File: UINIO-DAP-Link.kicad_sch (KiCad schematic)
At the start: 0 parts

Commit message: Start schematic drawing work.
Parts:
- added C1: 10nF, Capacitor_SMD:C_0402_1005Metric, symbol Uinio:CAP_0402
- added C2: 10uF, Capacitor_SMD:C_0402_1005Metric, symbol Uinio:CAP_0402
- added C3, C4: 20pF, symbol Device:C
- added J1: Conn_01x04_Male, symbol Connector:Conn_01x04_Male
- added J2, J?: Conn_02x05_Top_Bottom, symbol Connector_Generic:Conn_02x05_Top_Bottom
- added J?: Conn_02x10_Top_Bottom, symbol Connector_Generic:Conn_02x10_Top_Bottom
- added R1, R2, R3, R5: 10K, symbol Device:R
- added R4: 100R, symbol Device:R
- added U1: ME6211, Uinio:SOT-23-5_L3.0-W1.7-P0.95-LS2.8-BR, symbol Uinio:ME6211
- added U2: STM32F103C8T6, kicad_lceda:LQFP-48_L7.0-W7.0-P0.50-LS9.0-BL, symbol Uinio:STM32F103C8T6
- added USB1: USB_Type_C_16Pin, Uinio:USB-C-SMD_TYPEC-304J-BCP16, symbol Uinio:USB_Type_C_16Pin
- added Y1: Crystal_GND24, symbol Device:Crystal_GND24
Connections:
- new net: C1.2, U1.4 (NC)
- new net: U2.6 (PD1-OSC_OUT), Y1.1
- new net: C3.2, Y1.2
- new net: U2.5 (PD0-OSC_IN), Y1.3
- new net: C4.2, Y1.4
- new net: R3.1, U2.7 (NRST)
- new net: R4.2, U2.25 (PB12)
- new net: R5.1, U2.44 (BOOT0)
- new net BOOT1: R2.1, U2.20 (PB2)
- new net Download_SWCLK: J1.2 (Pin_2), U2.37 (PA14)
- new net Download_SWDIO: J1.3 (Pin_3), U2.34 (PA13)
- new net GND: C1.1, C2.1, C3.1, C4.1, J1.1 (Pin_1), J2.7 (Pin_7), J?.12 (Pin_12), J?.13 (Pin_13), J?.14 (Pin_14), J?.15 (Pin_15), J?.16 (Pin_16), J?.17 (Pin_17), J?.18 (Pin_18), J?.19 (Pin_19), J?.20 (Pin_20), J?.7 (Pin_7), R2.2, R5.2, U1.2 (Vss), U2.23 (VSS_1), U2.35 (VSS_2), U2.47 (VSS_3), U2.8 (VSSA), USB1.13 (GND), USB1.14 (GND), USB1.15 (GND), USB1.16 (GND), USB1.A1B12 (GND), USB1.B1A12 (GND)
- new net JTAG_TCK/SWCLK: J2.6 (Pin_6), U2.26 (PB13)
- new net JTAG_TDI: J2.5 (Pin_5), U2.17 (PA7)
- new net JTAG_TDO: J2.4 (Pin_4), U2.15 (PA5)
- new net JTAG_TMS/SWDIO: J2.8 (Pin_8), R4.1, U2.27 (PB14)
- new net JTAG_nTRST: J2.3 (Pin_3), R1.1, U2.18 (PB0)
- new net LED_BLUE: U2.42 (PB6)
- new net LED_RED: U2.30 (PA9)
- new net RESET: J?.8 (Pin_8)
- new net RTCK: J?.6 (Pin_6)
- new net TCK: J?.5 (Pin_5)
- new net TDI: J?.3 (Pin_3)
- new net TDO: J?.7 (Pin_7)
- new net TMS: J?.4 (Pin_4)
- new net USART2_RX: J2.2 (Pin_2), U2.13 (PA3)
- new net USART2_TX: J2.1 (Pin_1), U2.12 (PA2)
- new net USB_Data_N: U2.32 (PA11), USB1.A7 (DN1), USB1.B7 (DN2)
- new net USB_Data_P: U2.33 (PA12), USB1.A6 (DP1), USB1.B6 (DP2)
- new net USB_ENUM: U2.28 (PB15)
- new net VDD_3.3V: C2.2, J1.4 (Pin_4), J2.9 (Pin_9), R1.2, R3.2, U1.5 (Vout), U2.1 (VBAT), U2.24 (VDD_1), U2.36 (VDD_2), U2.48 (VDD_3), U2.9 (VDDA)
- new net VDD_5V: J2.10 (Pin_10), U1.1 (Vin), U1.3 (CE), USB1.A4B9 (VBUS), USB1.B4A9 (VBUS)
- new net VTref: J?.1 (Pin_1)
- new net _JTAG_TCK/SWCLK: J?.6 (Pin_6)
- new net _JTAG_TDI: J?.5 (Pin_5)
- new net _JTAG_TDO: J?.4 (Pin_4)
- new net _JTAG_TMS/SWDIO: J?.8 (Pin_8)
- new net _JTAG_nTRST: J?.3 (Pin_3)
- new net _USART2_RX: J?.2 (Pin_2)
- new net _USART2_TX: J?.1 (Pin_1)
- new net _VDD_3.3V: J?.9 (Pin_9)
- new net _VDD_5V: J?.10 (Pin_10)
- new net nTRST: J?.2 (Pin_2)
- no-connect marks 0 -> 25
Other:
- note added: "DAPLink 固件下载接口"
- note added: "JTAG/SWD 下载接口"
- note added: "ME6211 线性稳压器"
- note added: "STM32F103C8T6 最小系统"
- note added: "USB Type-C 接口"

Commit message: Update extends board design.
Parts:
- added D?: BLUE LED, symbol Device:LED
- added D? (x2): Blue LED, symbol Device:LED
- added J?: Conn_01x05_Male, symbol Connector:Conn_01x05_Male
- added J? (x2): Conn_01x02_Male, symbol Connector:Conn_01x02_Male
- added R? (x3): 1.5K, symbol Device:R
- added R? (x2): 22R, symbol Device:R
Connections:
- net GND: now also J?.9 (Pin_9), J?.1 (Pin_1), R?.1; no longer J?.7 (Pin_7)
- net _JTAG_TCK/SWCLK: now also J?.10 (Pin_10); no longer J?.6 (Pin_6)
- net _JTAG_TDI: now also R?.1; no longer J?.5 (Pin_5)
- net _JTAG_TDO: now also R?.1; no longer J?.4 (Pin_4)
- net _USART2_RX: now also J?.4 (Pin_4), J?.2 (Pin_2), R?.2; no longer J?.2 (Pin_2)
- net _USART2_TX: now also J?.5 (Pin_5), J?.3 (Pin_3), R?.2; no longer J?.1 (Pin_1)
- net _VDD_3.3V: now also J?.7 (Pin_7); no longer J?.9 (Pin_9)
- net _VDD_5V: now also J?.6 (Pin_6); no longer J?.10 (Pin_10)
- net _JTAG_nTRST renamed _JTAG_nTRST_Output
- new net: D?.1 (K), R?.2
- new net: J?.1 (Pin_1), R?.2
- new net: J?.2 (Pin_2), R?.2
- new net: D?.1 (K), R?.1 (x2)
- new net 3.3V_Input: D?.2 (A), D?.2 (A), D?.2 (A), J?.4 (Pin_4)
- new net 5V: J?.5 (Pin_5)
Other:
- note added: "3.3V_Input"
- note added: "3.3V_Output"
- moved on the sheet: C1, C2, C3, C4, J1, J2, J?, R1, R2, R3, R4, R5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

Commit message: Update PCB.
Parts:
- removed C1: 10nF, Capacitor_SMD:C_0402_1005Metric, symbol Uinio:CAP_0402
- removed C2: 10uF, Capacitor_SMD:C_0402_1005Metric, symbol Uinio:CAP_0402
- added C1: 10nF, Capacitor_SMD:C_0603_1608Metric, symbol Device:C
- added C2: 10uF, Capacitor_SMD:C_0603_1608Metric, symbol Device:C
- added C?: 0.1uF, Capacitor_SMD:C_0603_1608Metric, symbol Device:C
- C3, C4: footprint (none) -> Capacitor_SMD:C_0603_1608Metric
- D1: renamed from D?; value Blue LED -> LED Red; footprint (none) -> Capacitor_SMD:C_0603_1608Metric
- D2: renamed from D?; value Blue LED -> LED Blue; footprint (none) -> Capacitor_SMD:C_0603_1608Metric
- D3: renamed from D?; value BLUE LED -> LED Blue; footprint (none) -> Capacitor_SMD:C_0603_1608Metric
- J1: renamed from J?; footprint (none) -> Connector_PinHeader_2.54mm:PinHeader_1x05_P2.54mm_Vertical
- J2: renamed from J?; value Conn_02x10_Top_Bottom -> JTAG 输出; footprint (none) -> Connector_PinHeader_2.54mm:PinHeader_2x10_P2.54mm_Vertical
- J3: renamed from J?; value Conn_01x02_Male -> JTAG_nTRST 跳线选择; footprint (none) -> Connector_PinHeader_2.54mm:PinHeader_1x02_P2.54mm_Vertical
- J4: renamed from J?; value Conn_01x02_Male -> 3.3V 跳线选择; footprint (none) -> Connector_PinHeader_2.54mm:PinHeader_1x02_P2.54mm_Vertical
- J5: renamed from J?; value Conn_02x05_Top_Bottom -> SWD 输入; footprint (none) -> Connector_PinHeader_2.54mm:PinHeader_2x05_P2.54mm_Vertical
- J6: renamed from J1; value Conn_01x04_Male -> DAPLink 固件下载接口; footprint (none) -> Connector:FanPinHeader_1x04_P2.54mm_Vertical
- J7: renamed from J2; value Conn_02x05_Top_Bottom -> JTAG/SWD 下载接口; footprint (none) -> Connector_PinHeader_2.54mm:PinHeader_2x05_P2.54mm_Vertical
- R1, R2, R3, R4, R5: renamed from R?; footprint (none) -> Resistor_SMD:R_0603_1608Metric
- R10: renamed from R5; footprint (none) -> Resistor_SMD:R_0603_1608Metric
- R6: renamed from R1; footprint (none) -> Resistor_SMD:R_0603_1608Metric
- R7: renamed from R2; footprint (none) -> Resistor_SMD:R_0603_1608Metric
- R8: renamed from R3; footprint (none) -> Resistor_SMD:R_0603_1608Metric
- R9: renamed from R4; footprint (none) -> Resistor_SMD:R_0603_1608Metric
- U1: renamed from U2; footprint kicad_lceda:LQFP-48_L7.0-W7.0-P0.50-LS9.0-BL -> Uinio:LQFP-48_L7.0-W7.0-P0.50-LS9.0
- Y1: footprint (none) -> Crystal:Crystal_SMD_0603-4Pin_6.0x3.5mm
- renumbered U1 to V1
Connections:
- net 3.3V_Input: now also J4.1 (Pin_1)
- net GND: now also C1.1, C2.2, C?.2
- net VDD_3.3V: now also C2.1
- net _JTAG_nTRST_Output: now also J3.2 (Pin_2)
- net at V1.4 (NC): now also C1.2
- net at R8.1, U1.7 (NRST): now also C?.1
- net _JTAG_nTRST_Input: now reaches J3.1 (Pin_1)
- net 3.3V_Output: now reaches J2.11 (Pin_11)
- net 3.3V_Output: now also J4.2 (Pin_2)
- net LED_BLUE renamed LED Red
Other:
- note added: "JTAG 扩展板"
- note removed: "3.3V_Input"
- note removed: "3.3V_Output"
- moved on the sheet: D1, D2, D3, J3, J4, J5, J6, J7, R1, R2, R3, R4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

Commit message: Update PCB layout.
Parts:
- added D4: LED_Blue, LED_SMD:LED_0603_1608Metric, symbol Device:LED
- added D5: LED_Red, LED_SMD:LED_0603_1608Metric, symbol Device:LED
- added R11, R12: 10K, Resistor_SMD:R_0603_1608Metric, symbol Device:R
- D1: value LED Red -> LED_Red; footprint Capacitor_SMD:C_0603_1608Metric -> LED_SMD:LED_0603_1608Metric
- D2, D3: value LED Blue -> LED_Blue; footprint Capacitor_SMD:C_0603_1608Metric -> LED_SMD:LED_0603_1608Metric
- J1: value Conn_01x05_Male -> 扩展板串口 & 电源输出
- J2: value JTAG 输出 -> 扩展板 JTAG 输出; footprint Connector_PinHeader_2.54mm:PinHeader_2x10_P2.54mm_Vertical -> Connector_IDC:IDC-Header_2x10_P2.54mm_Horizontal
- J5: value SWD 输入 -> 扩展板 SWD 输入; footprint Connector_PinHeader_2.54mm:PinHeader_2x05_P2.54mm_Vertical -> Connector_IDC:IDC-Header_2x05_P2.54mm_Horizontal
- J6: footprint Connector:FanPinHeader_1x04_P2.54mm_Vertical -> Connector_PinHeader_2.54mm:PinHeader_1x04_P2.54mm_Vertical
- J7: footprint Connector_PinHeader_2.54mm:PinHeader_2x05_P2.54mm_Vertical -> Connector_IDC:IDC-Header_2x05_P2.54mm_Horizontal
- gave numbers to parts that had none: 1
- renumbered R8 to R6, R6 to R7, R7 to R8, V1 to U1, U1 to U2
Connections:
- net GND: now also R11.2, R12.2
- net LED Red: no longer names the net of U2.42 (PB6)
- net LED Red: now also D4.2 (A)
- net LED_RED: no longer names the net of U2.30 (PA9)
- net LED_RED: now also D5.2 (A)
- new net: D4.1 (K), R11.1
- new net: D5.1 (K), R12.1
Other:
- note added: "DAPLink 固件下载"
- note added: "SWD/JTAG 输出"
- note removed: "DAPLink 固件下载接口"
- note removed: "JTAG/SWD 下载接口"

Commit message: Update PCB layout.
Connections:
- net RESET is gone; now on net _JTAG_nTRST_Output: J2.8 (Pin_8)
- net TCK is gone; now on net _JTAG_TCK/SWCLK: J2.5 (Pin_5)
- net TDI is gone; now on net _JTAG_TDI: J2.3 (Pin_3)
- net TDO is gone; now on net _JTAG_TDO: J2.7 (Pin_7)
- net TMS is gone; now on net _JTAG_TMS/SWDIO: J2.4 (Pin_4)
- net VTref is gone; now on net 3.3V_Output: J2.1 (Pin_1)
- no-connect marks 25 -> 27
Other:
- moved on the sheet: J2, J3, J4, R4, R5

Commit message: Update PCB layout.
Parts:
- removed J5: 扩展板 SWD 输入, Connector_IDC:IDC-Header_2x05_P2.54mm_Horizontal, symbol Connector_Generic:Conn_02x05_Top_Bottom
- removed J7: JTAG/SWD 下载接口, Connector_IDC:IDC-Header_2x05_P2.54mm_Horizontal, symbol Connector_Generic:Conn_02x05_Top_Bottom
- added J5: 扩展板 SWD 输入, Connector_IDC:IDC-Header_2x05_P2.54mm_Horizontal, symbol Connector_Generic:Conn_02x05_Odd_Even
- added J7: JTAG/SWD 下载接口, Connector_IDC:IDC-Header_2x05_P2.54mm_Horizontal, symbol Connector_Generic:Conn_02x05_Odd_Even
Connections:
- net GND: now also J5.4 (Pin_4), J7.8 (Pin_8)
- net JTAG_TCK/SWCLK: now also J7.10 (Pin_10)
- net JTAG_TDI: now also J7.1 (Pin_1)
- net JTAG_TDO: now also J7.3 (Pin_3)
- net JTAG_TMS/SWDIO: now also J7.6 (Pin_6)
- net JTAG_nTRST: now also J7.5 (Pin_5)
- net USART2_RX: now also J7.7 (Pin_7)
- net USART2_TX: now also J7.9 (Pin_9)
- net VDD_3.3V: now also J7.4 (Pin_4)
- net VDD_5V: now also J7.2 (Pin_2)
- net _JTAG_TCK/SWCLK: now also J5.2 (Pin_2)
- net _JTAG_TMS/SWDIO: now also J5.6 (Pin_6)
- net _JTAG_nTRST_Output: now also J5.5 (Pin_5)
- net _USART2_RX: now also J5.3 (Pin_3)
- net _USART2_TX: now also J5.1 (Pin_1)
- net _VDD_3.3V: now also J5.8 (Pin_8)
- net _VDD_5V: now also J5.10 (Pin_10)
- net at R5.2: now also J5.9 (Pin_9)
- net at R4.2: now also J5.7 (Pin_7)
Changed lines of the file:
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@@
-    (stroke (width 0) (type default) (color 0 0 0 0))
-  )
-  (wire (pts (xy 128.27 175.26) (xy 121.92 175.26))
     (stroke (width 0) (type default) (color 0 0 0 0))
   )
@@
   )
   (wire (pts (xy 53.975 143.51) (xy 56.515 143.51))
+    (stroke (width 0) (type default) (color 0 0 0 0))
+  )
+  (wire (pts (xy 109.22 167.64) (xy 128.27 167.64))
     (stroke (width 0) (type default) (color 0 0 0 0))
   )
@@
     (stroke (width 0) (type default) (color 0 0 0 0))
   )
-  (wire (pts (xy 109.22 170.18) (xy 128.27 170.18))
-    (stroke (width 0) (type default) (color 0 0 0 0))
-  )
   (polyline (pts (xy 17.78 130.81) (xy 114.3 130.81))
     (stroke (width 0) (type default) (color 0 0 0 0))
@@
     (stroke (width 0) (type default) (color 0 0 0 0))
   )
+  (wire (pts (xy 124.46 177.8) (xy 128.27 177.8))
+    (stroke (width 0) (type default) (color 0 0 0 0))
+  )
   (wire (pts (xy 236.22 104.14) (xy 243.84 104.14))
     (stroke (width 0) (type default) (color 0 0 0 0))
@@
     (stroke (width 0) (type default) (color 0 0 0 0))
   )
-  (wire (pts (xy 124.46 177.8) (xy 128.27 177.8))
-    (stroke (width 0) (type default) (color 0 0 0 0))
-  )
   (polyline (pts (xy 114.3 16.51) (xy 114.3 57.15))
     (stroke (width 0) (type default) (color 0 0 0 0))
@@
   )
   (wire (pts (xy 93.98 185.42) (xy 90.17 185.42))
+    (stroke (width 0) (type default) (color 0 0 0 0))
+  )
+  (wire (pts (xy 121.92 175.26) (xy 128.27 175.26))
     (stroke (width 0) (type default) (color 0 0 0 0))
   )
@@
     (stroke (width 0) (type default) (color 0 0 0 0))
   )
+  (wire (pts (xy 109.22 170.18) (xy 128.27 170.18))
+    (stroke (width 0) (type default) (color 0 0 0 0))
+  )
   (wire (pts (xy 236.22 109.22) (xy 243.84 109.22))
     (stroke (width 0) (type default) (color 0 0 0 0))
   )
   (wire (pts (xy 93.98 172.72) (xy 93.98 185.42))
-    (stroke (width 0) (type default) (color 0 0 0 0))
-  )
-  (wire (pts (xy 109.22 167.64) (xy 128.27 167.64))
     (stroke (width 0) (type default) (color 0 0 0 0))
   )
@@
     (pin "4")
   )
-  (symbol (lib_id "power:GND") (at 242.57 76.2 90) (unit 1)
-    (in_bom yes) (on_board yes)
-    (property "Reference" "#PWR019" (id 0) (at 248.92 76.2 0)
-      (effects (font (size 1.27 1.27)) hide)
-    )
-    (property "Value" "GND" (id 1) (at 245.872 76.2 90)
-      (effects (font (size 1.27 1.27)) (justify right))
-    )
-    (property "Footprint" "" (id 2) (at 242.57 76.2 0)
-      (effects (font (size 1.27 1.27)) hide)
-    )
-    (property "Datasheet" "" (id 3) (at 242.57 76.2 0)
-      (effects (font (size 1.27 1.27)) hide)
-    )
-    (pin "1")
-  )
-  (symbol (lib_id "power:GND") (at 191.77 129.54 270) (unit 1)
-    (in_bom yes) (on_board yes)
-    (property "Reference" "#PWR016" (id 0) (at 185.42 129.54 0)
-      (effects (font (size 1.27 1.27)) hide)
-    )
-    (property "Value" "GND" (id 1) (at 188.722 129.54 90)
-      (effects (font (size 1.27 1.27)) (justify right))
-    )
-    (property "Footprint" "" (id 2) (at 191.77 129.54 0)
-      (effects (font (size 1.27 1.27)) hide)
-    )
-    (property "Datasheet" "" (id 3) (at 191.77 129.54 0)
-      (effects (font (size 1.27 1.27)) hide)
-    )
-    (pin "1")
-  )
-  (symbol (lib_id "Connector_Generic:Conn_02x05_Top_Bottom") (at 133.35 172.72 0) (mirror x) (unit 1)
-    (in_bom yes) (on_board yes)
-    (property "Reference" "J5" (id 0) (at 134.62 180.34 0))
-    (property "Value" "扩展板 SWD 输入" (id 1) (at 134.62 162.56 0))
+  (symbol (lib_id "Connector_Generic:Conn_02x05_Odd_Even") (at 133.35 172.72 0) (unit 1)
+    (in_bom yes) (on_board yes)
+    (property "Reference" "J5" (id 0) (at 134.62 164.465 0))
+    (property "Value" "扩展板 SWD 输入" (id 1) (at 134.62 180.975 0))
     (property "Footprint" "Connector_IDC:IDC-Header_2x05_P2.54mm_Horizontal" (id 2) (at 133.35 172.72 0)
       (effects (font (size 1.27 1.27)) hide)
@@
     (pin "9")
   )
+  (symbol (lib_id "power:GND") (at 242.57 76.2 90) (unit 1)
+    (in_bom yes) (on_board yes)
+    (property "Reference" "#PWR019" (id 0) (at 248.92 76.2 0)
+      (effects (font (size 1.27 1.27)) hide)
+    )
+    (property "Value" "GND" (id 1) (at 245.872 76.2 90)
+      (effects (font (size 1.27 1.27)) (justify right))
+    )
+    (property "Footprint" "" (id 2) (at 242.57 76.2 0)
+      (effects (font (size 1.27 1.27)) hide)
+    )
+    (property "Datasheet" "" (id 3) (at 242.57 76.2 0)
+      (effects (font (size 1.27 1.27)) hide)
+    )
+    (pin "1")
+  )
+  (symbol (lib_id "power:GND") (at 191.77 129.54 270) (unit 1)
+    (in_bom yes) (on_board yes)
+    (property "Reference" "#PWR016" (id 0) (at 185.42 129.54 0)
+      (effects (font (size 1.27 1.27)) hide)
+    )
+    (property "Value" "GND" (id 1) (at 188.722 129.54 90)
+      (effects (font (size 1.27 1.27)) (justify right))
+    )
+    (property "Footprint" "" (id 2) (at 191.77 129.54 0)
+      (effects (font (size 1.27 1.27)) hide)
+    )
+    (property "Datasheet" "" (id 3) (at 191.77 129.54 0)
+      (effects (font (size 1.27 1.27)) hide)
+    )
+    (pin "1")
+  )
   (symbol (lib_id "power:GND") (at 88.9 95.25 90) (unit 1)
     (in_bom yes) (on_board yes)
@@
     (pin "1")
     (pin "2")
-  )
-  (symbol (lib_id "Connector_Generic:Conn_02x05_Top_Bottom") (at 231.14 34.29 0) (unit 1)
-    (in_bom yes) (on_board yes)
-    (property "Reference" "J7" (id 0) (at 232.41 25.4 0))
-    (property "Value" "JTAG/SWD 下载接口" (id 1) (at 232.41 43.18 0))
-    (property "Footprint" "Connector_IDC:IDC-Header_2x05_P2.54mm_Horizontal" (id 2) (at 231.14 34.29 0)
-      (effects (font (size 1.27 1.27)) hide)
-    )
-    (property "Datasheet" "~" (id 3) (at 231.14 34.29 0)
-      (effects (font (size 1.27 1.27)) hide)
-    )
-    (pin "1")
-    (pin "10")
-    (pin "2")
-    (pin "3")
-    (pin "4")
-    (pin "5")
-    (pin "6")
-    (pin "7")
-    (pin "8")
-    (pin "9")
   )
   (symbol (lib_id "Device:R") (at 257.81 83.82 90) (unit 1)
@@
     (pin "1")
   )
+  (symbol (lib_id "Connector_Generic:Conn_02x05_Odd_Even") (at 231.14 34.29 0) (mirror x) (unit 1)
+    (in_bom yes) (on_board yes)
+    (property "Reference" "J7" (id 0) (at 232.41 42.545 0))
+    (property "Value" "JTAG/SWD 下载接口" (id 1) (at 232.41 26.035 0))
+    (property "Footprint" "Connector_IDC:IDC-Header_2x05_P2.54mm_Horizontal" (id 2) (at 231.14 34.29 0)
+      (effects (font (size 1.27 1.27)) hide)
+    )
+    (property "Datasheet" "~" (id 3) (at 231.14 34.29 0)
+      (effects (font (size 1.27 1.27)) hide)
+    )
+    (pin "1")
+    (pin "10")
+    (pin "2")
+    (pin "3")
+    (pin "4")
+    (pin "5")
+    (pin "6")
+    (pin "7")
+    (pin "8")
+    (pin "9")
+  )
   (sheet_instances
     (path "/" (page "1"))
@@
       (reference "J4") (unit 1) (value "3.3V 跳线选择") (footprint "Connector_PinHeader_2.54mm:PinHeader_1x02_P2.54mm_Vertical")
     )
-    (path "/a20b6086-0190-4aea-9391-2523a128aae2"
+    (path "/82d08633-7082-488c-bc13-6af6e7a4e7be"
       (reference "J5") (unit 1) (value "扩展板 SWD 输入") (footprint "Connector_IDC:IDC-Header_2x05_P2.54mm_Horizontal")
     )
@@
       (reference "J6") (unit 1) (value "DAPLink 固件下载接口") (footprint "Connector_PinHeader_2.54mm:PinHeader_1x04_P2.54mm_Vertical")
     )
-    (path "/c0a1c4ff-1649-4b4f-ad33-b983cfa7c049"
+    (path "/fa9e8a35-4445-47c5-9c77-266de9cdabc5"
       (reference "J7") (unit 1) (value "JTAG/SWD 下载接口") (footprint "Connector_IDC:IDC-Header_2x05_P2.54mm_Horizontal")
     )

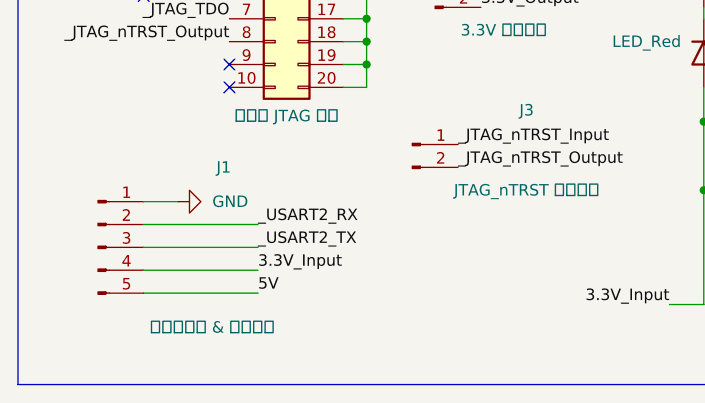
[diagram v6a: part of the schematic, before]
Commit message: Preliminarily completed the PCB layout.
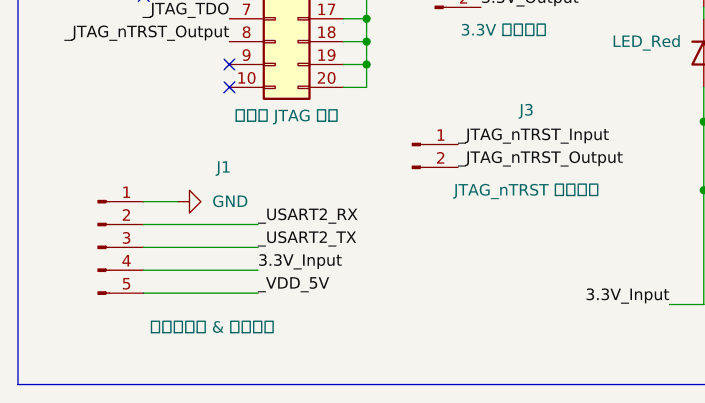
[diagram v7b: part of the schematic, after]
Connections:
- net 5V is gone; now on net _VDD_5V: J1.5 (Pin_5)
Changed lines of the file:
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@@
     (effects (font (size 1.27 1.27)) (justify right bottom))
+  )
+  (label "_VDD_5V" (at 44.45 184.15 0)
+    (effects (font (size 1.27 1.27)) (justify left bottom))
   )
   (label "VDD_3.3V" (at 160.02 38.1 0)
@@
     (effects (font (size 1.27 1.27)) (justify right bottom))
   )
-  (label "5V" (at 44.45 184.15 0)
-    (effects (font (size 1.27 1.27)) (justify left bottom))
-  )
   (label "3.3V_Output" (at 69.215 152.4 0)

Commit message: Release UINIO-DAP-Link 1.0.0.
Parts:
- removed J2: 扩展板 JTAG 输出, Connector_IDC:IDC-Header_2x10_P2.54mm_Horizontal, symbol Connector_Generic:Conn_02x10_Top_Bottom
- added J2: 扩展板 JTAG 输出, Connector_IDC:IDC-Header_2x10_P2.54mm_Horizontal, symbol Connector_Generic:Conn_02x10_Odd_Even
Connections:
- net 3.3V_Input: now also J1.3 (Pin_3); no longer J1.4 (Pin_4)
- net 3.3V_Output: now also J2.1 (Pin_1), J2.2 (Pin_2)
- net GND: now also J1.4 (Pin_4), J5.2 (Pin_2), J7.10 (Pin_10), J2.10 (Pin_10), J2.12 (Pin_12), J2.14 (Pin_14), J2.16 (Pin_16), J2.18 (Pin_18), J2.20 (Pin_20), J2.4 (Pin_4), J2.6 (Pin_6), J2.8 (Pin_8); no longer J1.1 (Pin_1), J5.4 (Pin_4), J7.8 (Pin_8)
- net JTAG_TCK/SWCLK: now also J7.8 (Pin_8); no longer J7.10 (Pin_10)
- net RTCK: now also J2.11 (Pin_11)
- net _JTAG_TCK/SWCLK: now also J5.4 (Pin_4), J2.9 (Pin_9); no longer J5.2 (Pin_2)
- net _JTAG_TDI: now also J2.5 (Pin_5)
- net _JTAG_TDO: now also J2.13 (Pin_13)
- net _JTAG_TMS/SWDIO: now also J2.7 (Pin_7)
- net _USART2_RX: now also J1.1 (Pin_1); no longer J1.2 (Pin_2)
- net _USART2_TX: now also J1.2 (Pin_2); no longer J1.3 (Pin_3)
- net nTRST: now also J2.3 (Pin_3)
- net _JTAG_nTRST_Input renamed _JTAG_nSRST_Input
- net _JTAG_nTRST_Output renamed _JTAG_nSRST_Output
- net _JTAG_nSRST_Output: now also J2.15 (Pin_15)
